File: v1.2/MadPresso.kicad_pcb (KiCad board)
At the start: 2 copper layers, 108 x 57.5 mm, 75 parts, among them J1 Conn_01x07, J2 Conn_01x03, J3 Conn_01x02, J4 Conn_01x04, Q1 BC847, Q2 BSS84, Q3 T835-600B, Q4 2N7002, Q5 T835-600B, Q6 2N7002, Q7 T835-600B, Q8 2N7002, U1 LTV-356T, U2 ADC101C021CIMK, U3 WeMos_D1_mini, U4 MID400, U5 MID400, U6 TLP160G, U7 TLP160G, U8 TLP160G

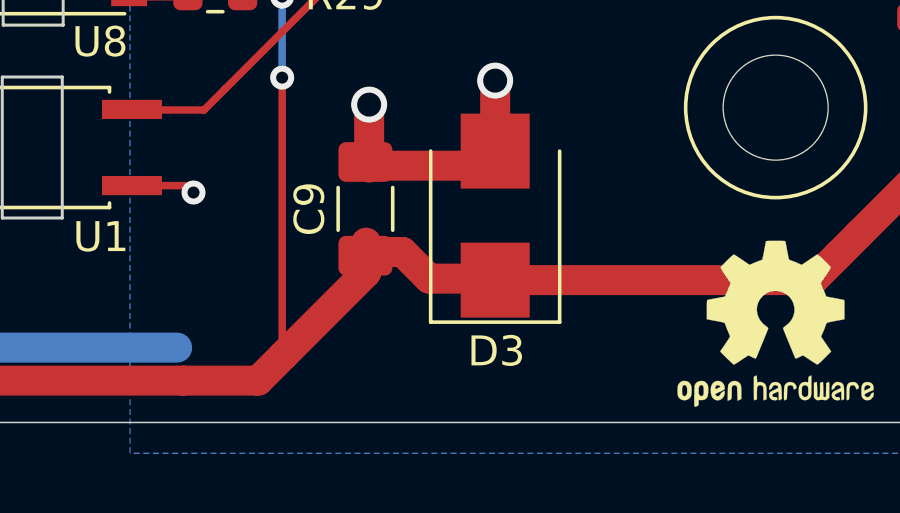
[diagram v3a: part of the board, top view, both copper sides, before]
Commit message: re-add kicad logo
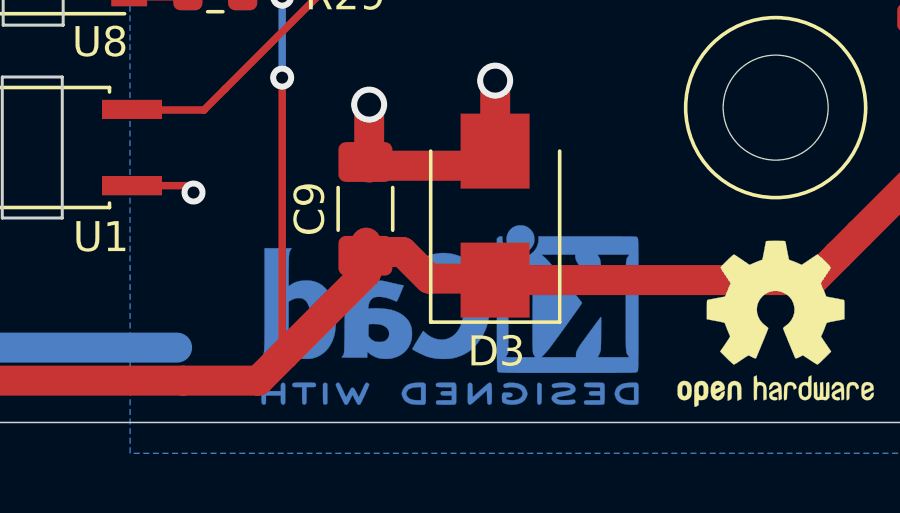
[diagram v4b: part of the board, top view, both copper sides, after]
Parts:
- added REF**: KiCad-Logo2_5mm_Copper, Symbol:KiCad-Logo2_5mm_Copper, B.Cu at (81.9, 53.9)

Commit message: some minor details
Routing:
- net GND: track 85.1 -> 83.0 mm
- net +5V: track 182.1 -> 183.3 mm
